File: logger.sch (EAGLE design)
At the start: 75 parts, among them IC1 LTC4412, J1 POWER_JACKPTH, Q1 FDN360P, Q2 FDN360P, Q3 2N7002PW, Q4 2N7002PW, U1 DS3231MZ/V+T, U2 FT231X-Q

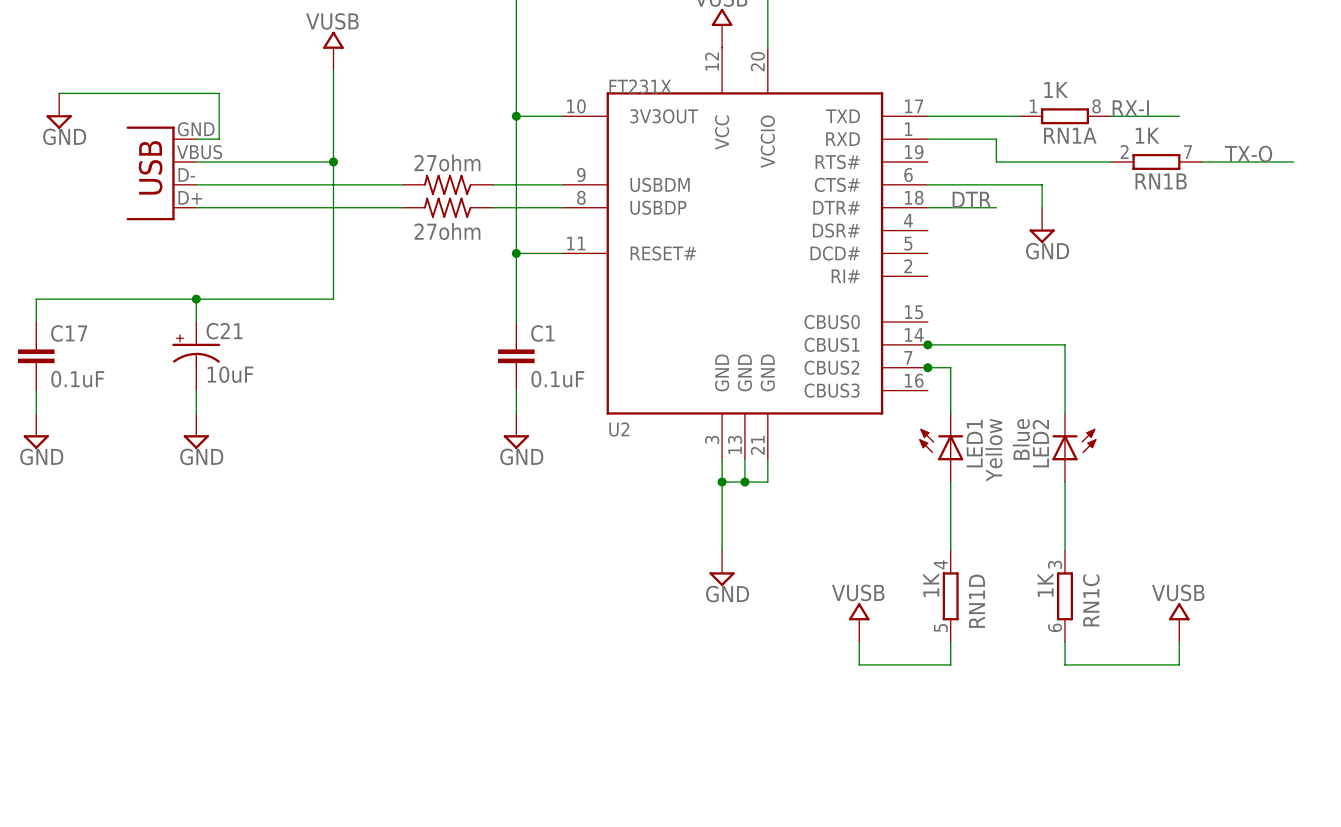
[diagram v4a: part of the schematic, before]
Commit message: 33pF decoupling on USB data; Rx Tx LED flip
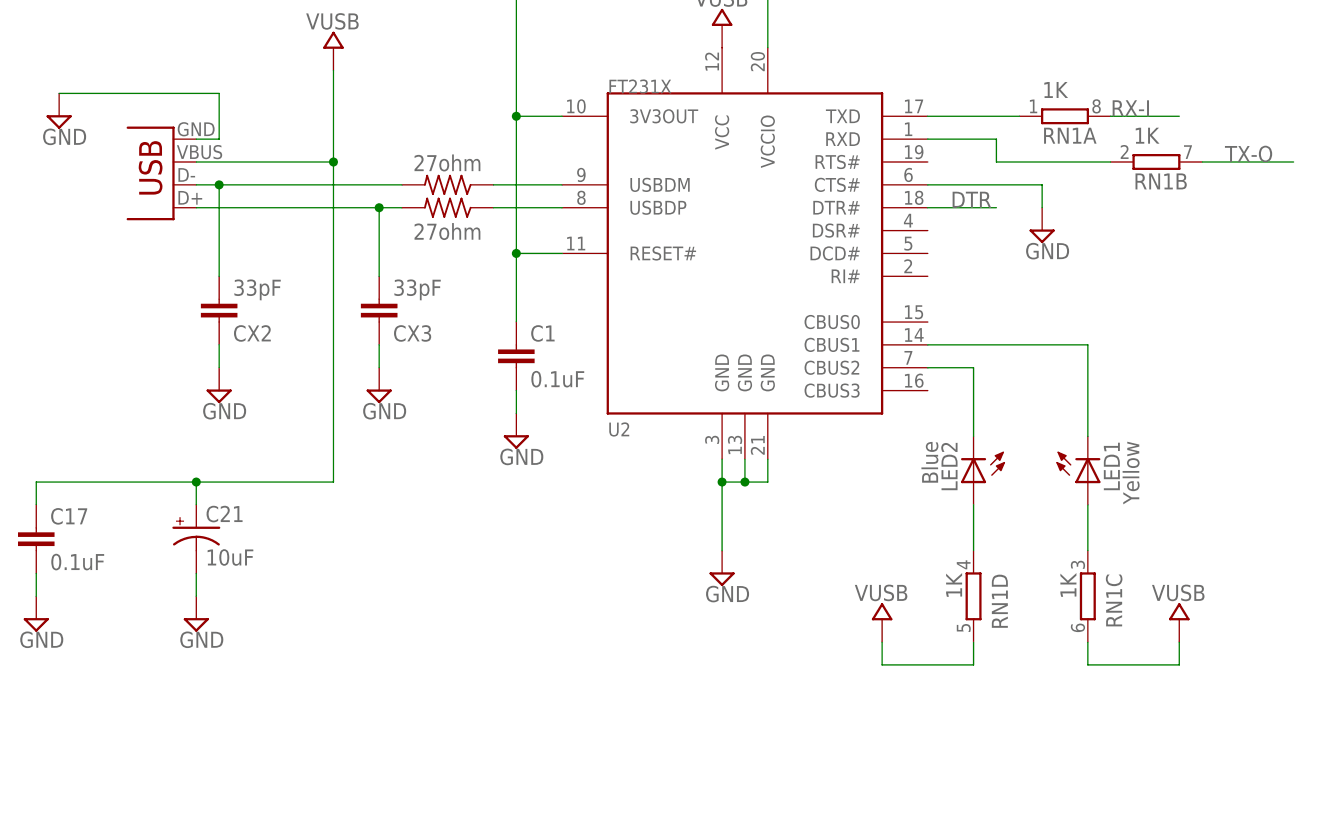
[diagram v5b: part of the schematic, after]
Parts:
- added CX2, CX3: 33pF, resistor:C-EUC0603
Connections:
- net GND: now also CX2.1, CX3.1
- net N$10: now also LED1.C, U2.CBUS1; no longer LED2.A, RN1C.1
- net N$3: now also CX3.2
- net N$4: now also CX2.2
- net N$5: now also LED2.A, RN1D.1; no longer LED1.C, U2.CBUS2
- net N$6: now also U2.CBUS2; no longer U2.CBUS1
- net N$9: now also RN1C.1; no longer RN1D.1
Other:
- moved on the sheet: C17, C21, LED1, LED2, RN1C, RN1D

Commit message: Final files for V2.0!
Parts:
- COUT1: value 1uF -> 0.1uF
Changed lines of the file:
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@@
 <part name="SUPPLY48" library="supply2" deviceset="GND" device=""/>
 <part name="SUPPLY49" library="supply2" deviceset="GND" device=""/>
-<part name="COUT1" library="rcl" deviceset="C-EU" device="C0603" value="1uF"/>
+<part name="COUT1" library="rcl" deviceset="C-EU" device="C0603" value="0.1uF"/>
 <part name="D2" library="semicon-smd-ipc" deviceset="DIODE_AC-CA_" device="" value="BAT54C"/>
 <part name="LOG" library="SparkFun-Electromechanical" deviceset="SWITCH-MOMENTARY-2" device="PTH" value="LOG"/>

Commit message: updated schematic layout, added frames
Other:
- note added: "1/4"
- note added: "2.0"
- note added: "2/4"
- note added: "3/4"
- note added: "4/4"
- note added: "ALOG"
- note added: "MICROCONTROLLER"
- note added: "POWER MANAGEMENT & DECOUPLING"
- note added: "REAL TIME CLOCK"
- note added: "SD CARD AND LEVEL SHIFTER"
- note added: "USB & ISP"
- note added: "USER IO & REFERENCE RESISTORS"
- moved on the sheet: 3.3_SENSE, 5V_CHARGE_PUMP, A0, A1, A2, A3, A6, A7, ADECOUP, C1, C14A, C14B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
